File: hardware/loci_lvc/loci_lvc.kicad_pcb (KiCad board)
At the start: 2 copper layers, 110 x 50 mm, 25 parts, among them Q1 BSS138, U1 SN74LVCC3245APW, U2 SN74LVCC3245APW, U3 SN74LVCC3245APW, U4 SN74LVCC3245APW, U5 SN74LVCC3245APW

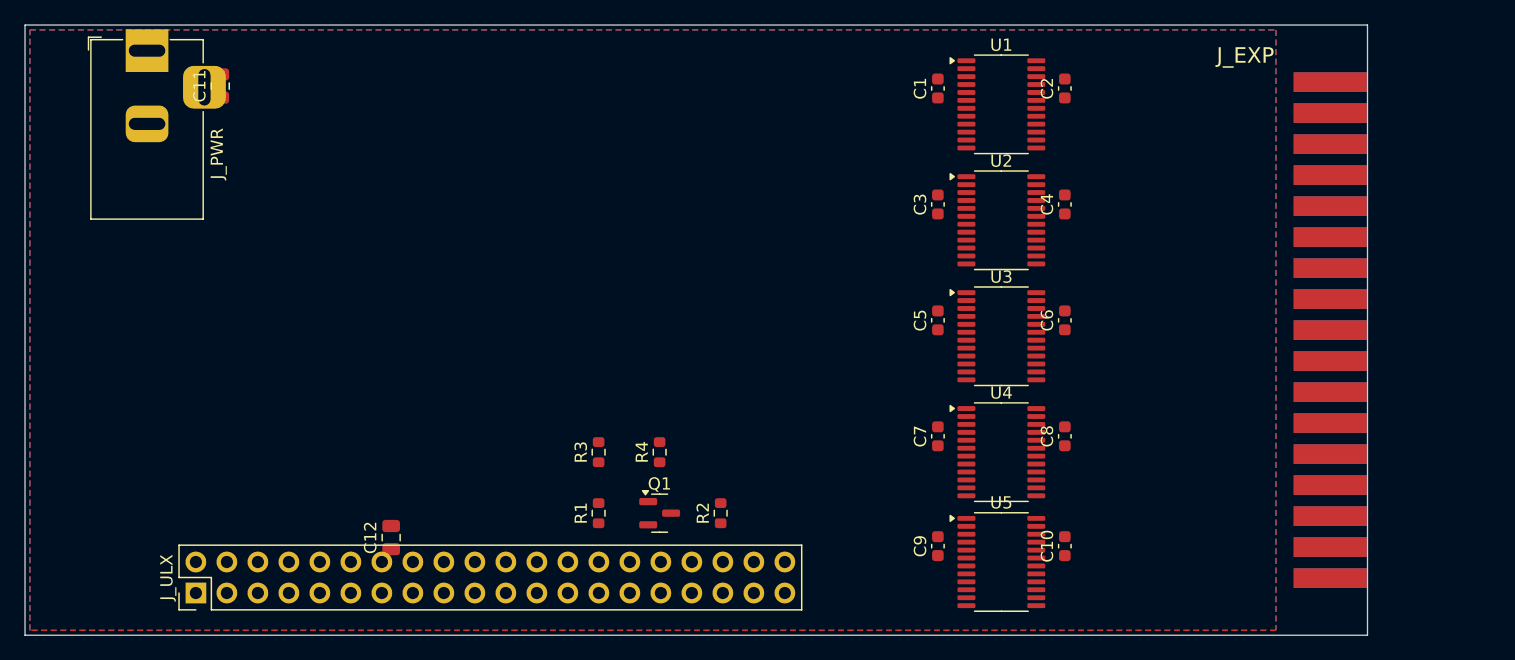
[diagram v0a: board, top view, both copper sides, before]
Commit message: Modem ESP32 v0.3 : AT$SCAN (wificonf.bas) + ATDISKRD (loci-webdisk) + robustesse
AT$SCAN au format attendu par wificonf.bas ; ATDISKRD au protocole exact
de ~/loci-webdisk (+DISK:<len> framing, corps brut, range en query) ;
garde globale anti-crash ; dispatch ATDISKRD avant ATD (le bug : la
commande tombait dans la numérotation). Réinstallé et testé sur l'ESP32.
PCB loci_lvc : correction des collisions C11/jack et C12/J_ULX.
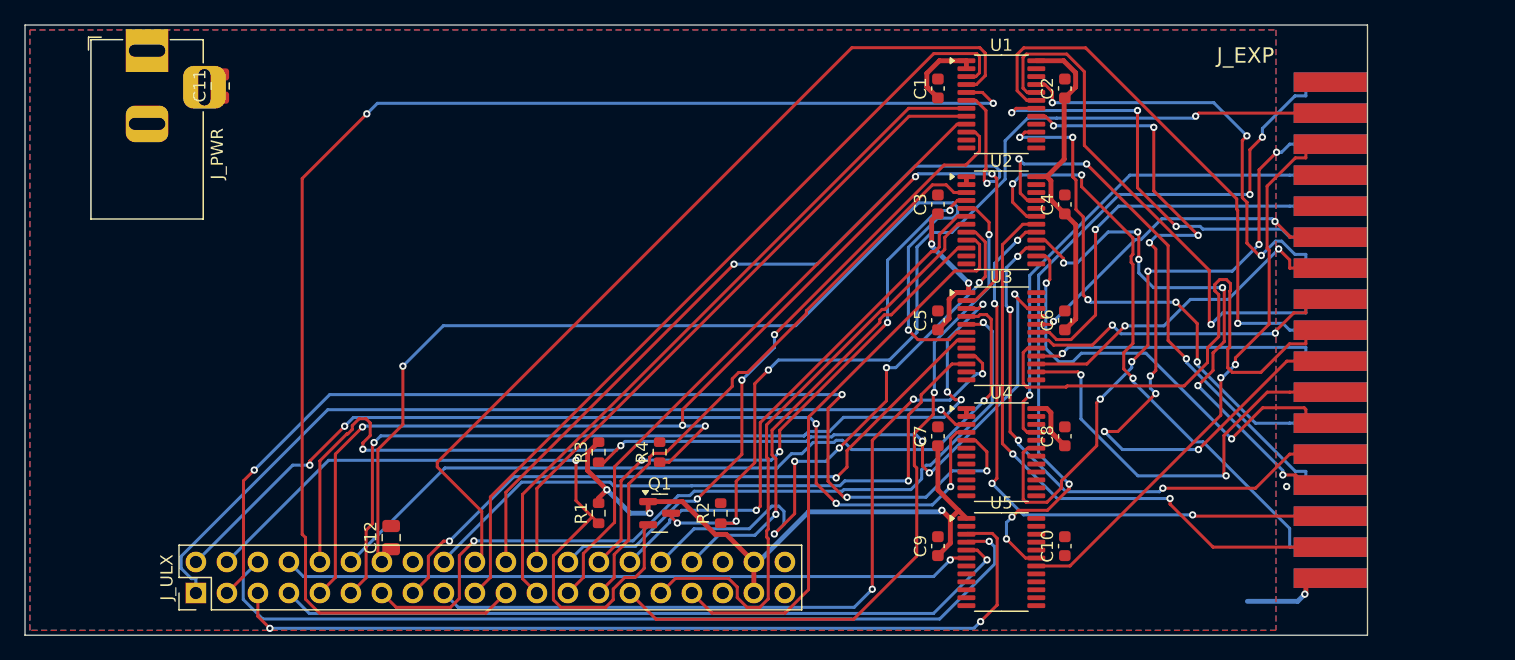
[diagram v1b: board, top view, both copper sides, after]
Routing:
- net A2: track 0.00 -> 113.9 mm, vias 0 -> 2
- net XCVR_DIR: track 0.00 -> 94.8 mm, vias 0 -> 5
- net XCVR_OE_n: track 0.00 -> 88.5 mm, vias 0 -> 5
- net IO_n: track 0.00 -> 87.4 mm, vias 0 -> 4
- net D3: track 0.00 -> 86.0 mm, vias 0 -> 2
- net RST5_n: track 0.00 -> 79.4 mm, vias 0 -> 4
- net PHI2: track 0.00 -> 78.8 mm, vias 0 -> 5
- net +3V3: track 0.00 -> 74.9 mm, vias 0 -> 5
- net D0: track 0.00 -> 74.1 mm, vias 0 -> 4
- net RW: track 0.00 -> 73.5 mm, vias 0 -> 1
- net A1: track 0.00 -> 72.8 mm
- net IRQ_n: track 0.00 -> 71.9 mm, vias 0 -> 2
- net ROMDIS_n: track 0.00 -> 71.6 mm, vias 0 -> 1
- net D2: track 0.00 -> 68.3 mm, vias 0 -> 2
- net A3: track 0.00 -> 67.2 mm, vias 0 -> 2
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
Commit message: ACIA 6551 : FIFO RX 4 Ko (anti-overrun) + DCD/DSR présents — liaison Oric-modem validée carte
Diagnostic sur carte (PEEK #31D = 28 : OK du modem reçu + OVRN) : l'ACIA
n'avait qu'un octet de tampon face au modem 115200, une boucle BASIC lit
~1000x plus lentement -> presque tout débordait (wificonf/term muets).
Équivalent du --serial-buffer 4096 de l'émulateur de référence : FIFO
BRAM 4 Ko show-ahead derrière le registre RDR, OVRN seulement si pleine,
purge au reset programmé. DCD/DSR câblés à 1 (réf. acia6551.c : true à
l'init). tb_acia : rafale 64 octets lue lentement, ordre et complétude.
Suite 20/20. Aussi : wificonf vise $0380 (LOCI) -> version ULX3S $031C
préparée (ligne 80 : DA=796...).
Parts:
- moved C11 9.43 mm to (24.0, 10.0)
- moved C12 4.00 mm to (30.0, 38.0)
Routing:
- net +5V: track 32.4 -> 185.1 mm, vias 0 -> 7
- net IO_n: track 87.4 -> 0.00 mm, vias 4 -> 0
- net A1: track 72.8 -> 0.00 mm
- net A7: track 54.3 -> 122.7 mm, vias 3 -> 2
- net D2: track 68.3 -> 0.00 mm, vias 2 -> 0
- net A3: track 67.2 -> 0.00 mm, vias 2 -> 0
- net D6: track 62.2 -> 0.00 mm, vias 3 -> 0
- net A10: track 58.8 -> 0.00 mm, vias 2 -> 0
- net D4: track 55.8 -> 0.00 mm, vias 2 -> 0
- net D5: track 0.00 -> 55.8 mm, vias 0 -> 1
- net A5: track 53.9 -> 0.00 mm
- net A6: track 52.4 -> 0.00 mm
- net IO5_n: track 50.3 -> 0.00 mm, vias 5 -> 0
- net A5V12: track 49.6 -> 0.00 mm, vias 4 -> 0
- net +3V3: track 74.9 -> 124.4 mm, vias 5 -> 0
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
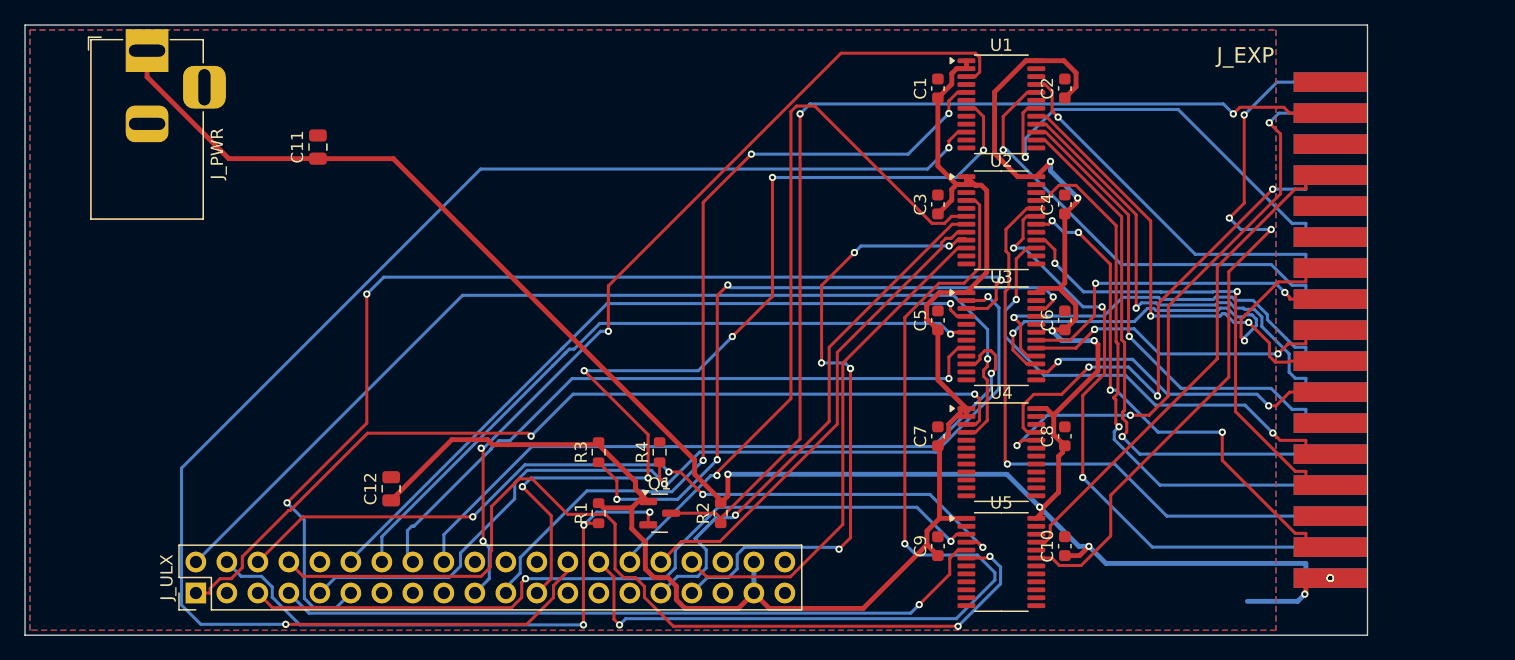
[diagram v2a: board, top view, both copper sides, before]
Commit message: Backlog : pivot berceau PCBA (US3.0b), variante B loci_lvc gelée
Le berceau (voie de fabrication retenue, convergée avec ulx3s2Loci) passe
en tête : il reste la table gp/gn <-> broches J1/J2 (KiCad emard/ulx3s),
le gen_pcb berceau et un routage freerouting (plus d'espace sans peigne).
La carte peigne garde son outillage mais son A* de finition produit des
courts — non aboutie, gelée en l'état.
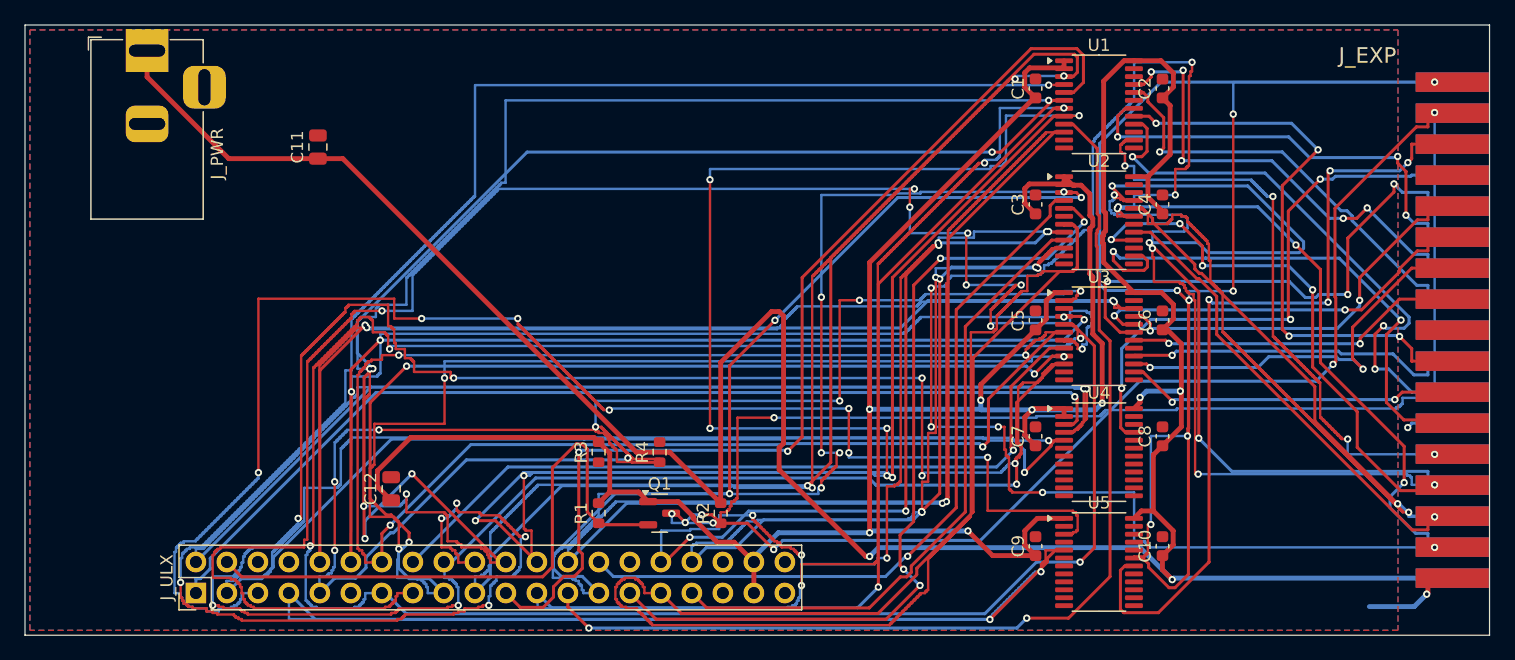
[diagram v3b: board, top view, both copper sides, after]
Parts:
- moved C1 8.00 mm to (82.8, 5.20)
- moved C10 8.00 mm to (93.2, 42.7)
- moved C2 8.00 mm to (93.2, 5.20)
- moved C3 8.00 mm to (82.8, 14.7)
- moved C4 8.00 mm to (93.2, 14.7)
- moved C5 8.00 mm to (82.8, 24.2)
- moved C6 8.00 mm to (93.2, 24.2)
- moved C7 8.00 mm to (82.8, 33.7)
- moved C8 8.00 mm to (93.2, 33.7)
- moved C9 8.00 mm to (82.8, 42.7)
- moved U1 8.00 mm to (88.0, 6.50)
- moved U2 8.00 mm to (88.0, 16.0)
- moved U3 8.00 mm to (88.0, 25.5)
- moved U4 8.00 mm to (88.0, 35.0)
- moved U5 8.00 mm to (88.0, 44.0)
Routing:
- net A3: track 0.00 -> 212.6 mm, vias 0 -> 8
- net A5: track 0.00 -> 192.3 mm, vias 0 -> 8
- net D2: track 0.00 -> 182.0 mm, vias 0 -> 5
- net A1: track 0.00 -> 168.6 mm, vias 0 -> 6
- net D6: track 0.00 -> 161.7 mm, vias 0 -> 7
- net IO_n: track 0.00 -> 159.4 mm, vias 0 -> 3
- net A8: track 0.00 -> 150.3 mm, vias 0 -> 9
- net D4: track 0.00 -> 148.9 mm, vias 0 -> 8
- net D7: track 58.1 -> 206.6 mm, vias 1 -> 9
- net A5V10: track 48.5 -> 172.4 mm, vias 3 -> 11
- net XCVR_OE_n: track 56.9 -> 174.1 mm
- net RST5_n: track 83.0 -> 185.1 mm, vias 2 -> 8
- net A0: track 71.6 -> 172.2 mm, vias 3 -> 5
- net D1: track 60.3 -> 157.8 mm, vias 1 -> 4
- net A12: track 46.2 -> 139.4 mm, vias 1 -> 0
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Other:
- board size 110 x 50 mm -> 120 x 50 mm
